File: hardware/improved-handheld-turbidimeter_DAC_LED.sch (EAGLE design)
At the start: 14 parts

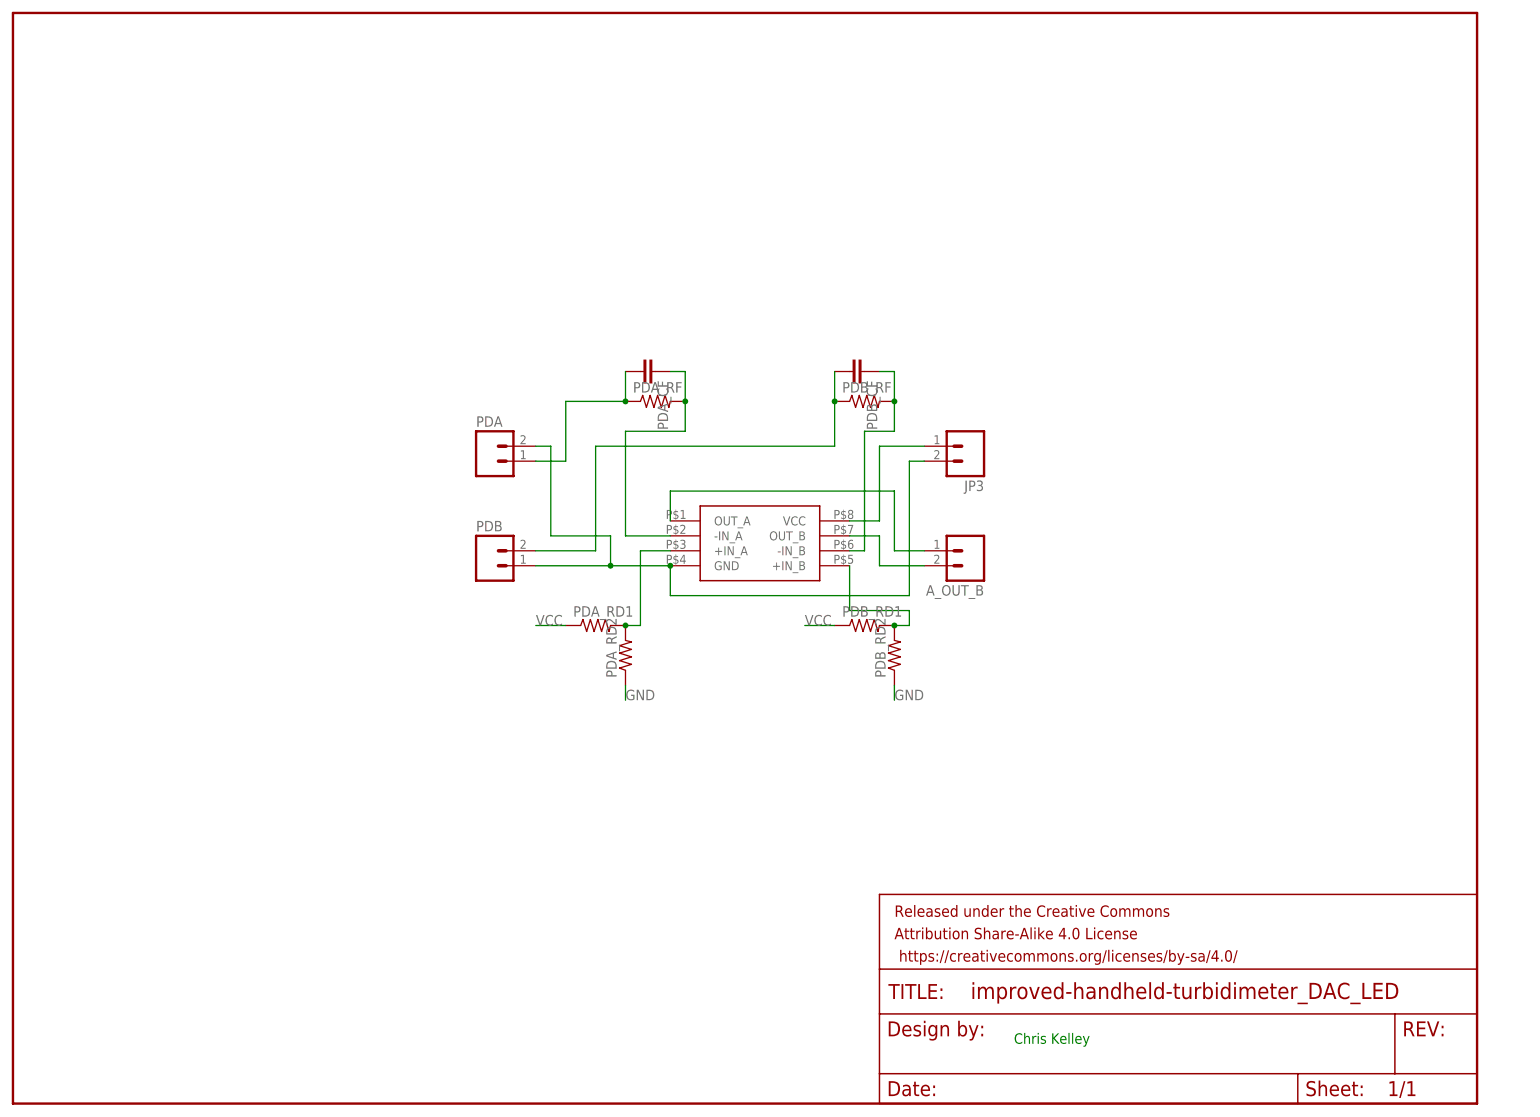
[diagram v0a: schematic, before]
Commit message: new and updated component boards
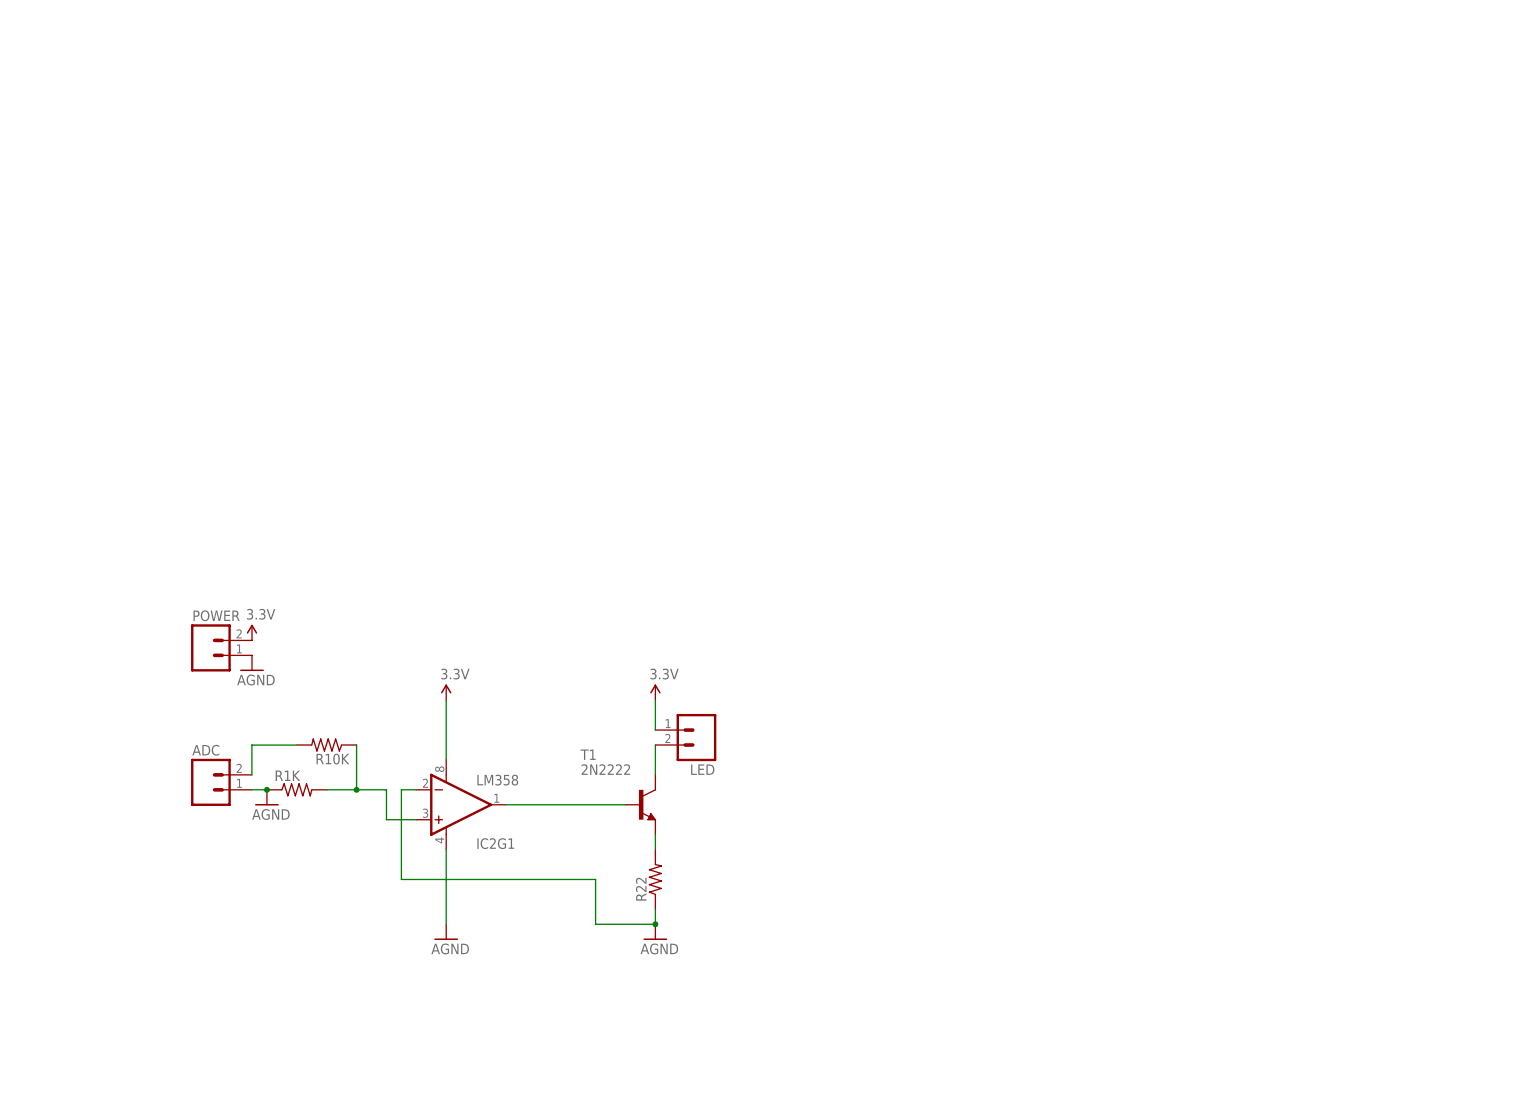
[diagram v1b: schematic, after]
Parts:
- removed A_OUT_B, JP3, PDA, PDB: (no value), SparkFun-Connectors:M02PTH
- removed FRAME1: FRAME-LETTER, SparkFun-Aesthetics:FRAME-LETTER
- removed PDA_CF, PDB_CF: (no value), SparkFun-Passives:CAP0603-CAP
- removed PDA_RD1, PDA_RD2, PDA_RF, PDB_RD1, PDB_RD2, PDB_RF: (no value), SparkFun-Passives:RESISTOR0603-RES
- removed U$2: ADA4528-2, awqua_eagle_library:ADA4528-2
- added ADC, LED, POWER: (no value), SparkFun-Connectors:M02PTH
- added IC2: LM358, SparkFun-AnalogIC:LM358
- added R10K, R1K, R22: (no value), SparkFun-Passives:RESISTOR0603-RES
- added T1: 2N2222, adafruit:2N2222
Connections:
- removed net GND: JP3.2, PDA.2, PDA_RD2.1, PDB.1, PDB_RD2.1, U$2.GND
- removed net N$4: PDB_CF.1, PDB_RF.2, U$2.-IN_B
- removed net OUTA: A_OUT_B.1, U$2.OUT_A
- removed net OUTB: A_OUT_B.2, U$2.OUT_B
- removed net VCC: JP3.1, PDA_RD1.1, PDB_RD1.1, U$2.VCC
- new net 3.3V: IC2G1.V+, LED.1, POWER.2
- new net AGND: ADC.1, IC2G1.-IN, IC2G1.V-, POWER.1, R1K.1, R22.1
- net N$1: now also IC2G1.OUT, T1.B; no longer PDA.1, PDA_CF.2, PDA_RF.1
- net N$2: now also LED.2, T1.C; no longer PDA_CF.1, PDA_RF.2, U$2.-IN_A
- net N$3: now also R22.2, T1.E; no longer PDB.2, PDB_CF.2, PDB_RF.1
- net N$5: now also ADC.2, R10K.2; no longer PDA_RD1.2, PDA_RD2.2, U$2.+IN_A
- net N$6: now also IC2G1.+IN, R10K.1, R1K.2; no longer PDB_RD1.2, PDB_RD2.2, U$2.+IN_B
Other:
- note removed: "Chris Kelley"
